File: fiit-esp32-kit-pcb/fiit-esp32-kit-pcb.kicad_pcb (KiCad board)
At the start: 2 copper layers, 25.4 x 75 mm, 79 parts, among them J1 Conn_01x22_Pin, J2 Conn_01x22_Pin, J3 Conn_ARM_JTAG_SWD_10, J4 Conn_01x06_Pin, J5 USB_C_Receptacle_USB2.0, J6 USB_C_Receptacle_USB2.0, Q1 MMDT3904, Q2 SFH320, SW1 SPST NO, SW2 SPST NO, SW3 SPST NO, SW4 SPST NO, SW5 SPST NO, U1 ESP32-S3-WROOM-1, U2 SY8089AAAC, U3 CP2102N-Axx-xQFN28, U4 AHT20

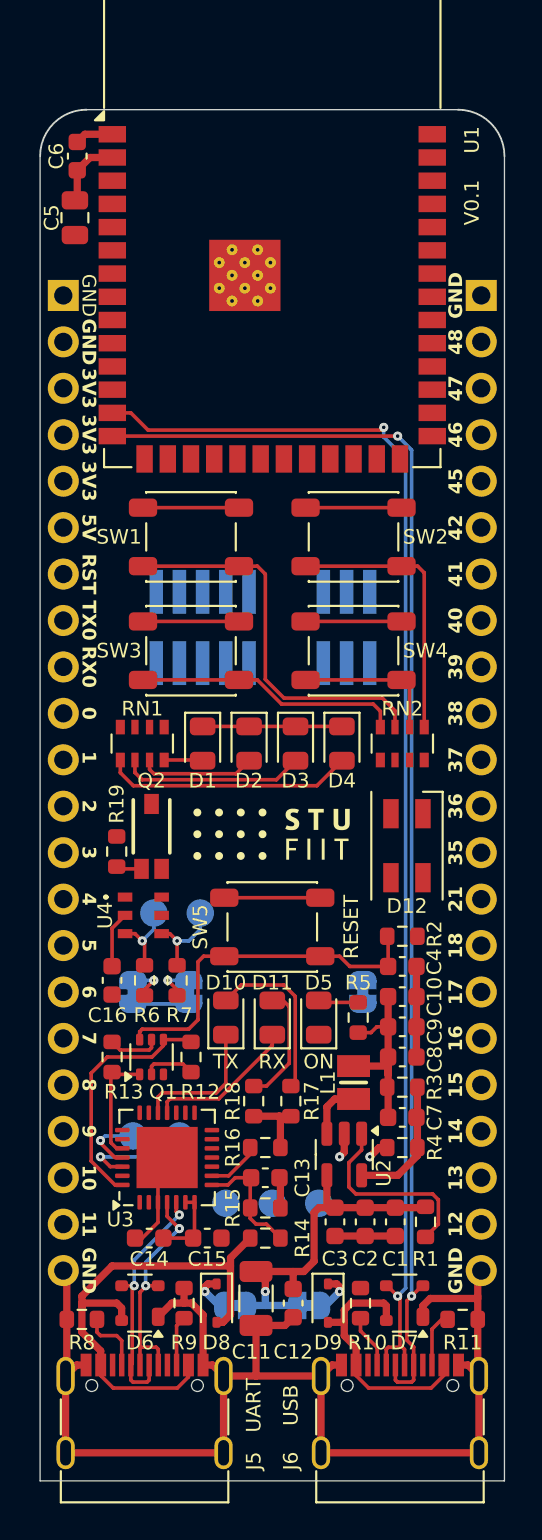
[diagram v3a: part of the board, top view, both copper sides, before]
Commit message: added some tracks (unrouted 76)
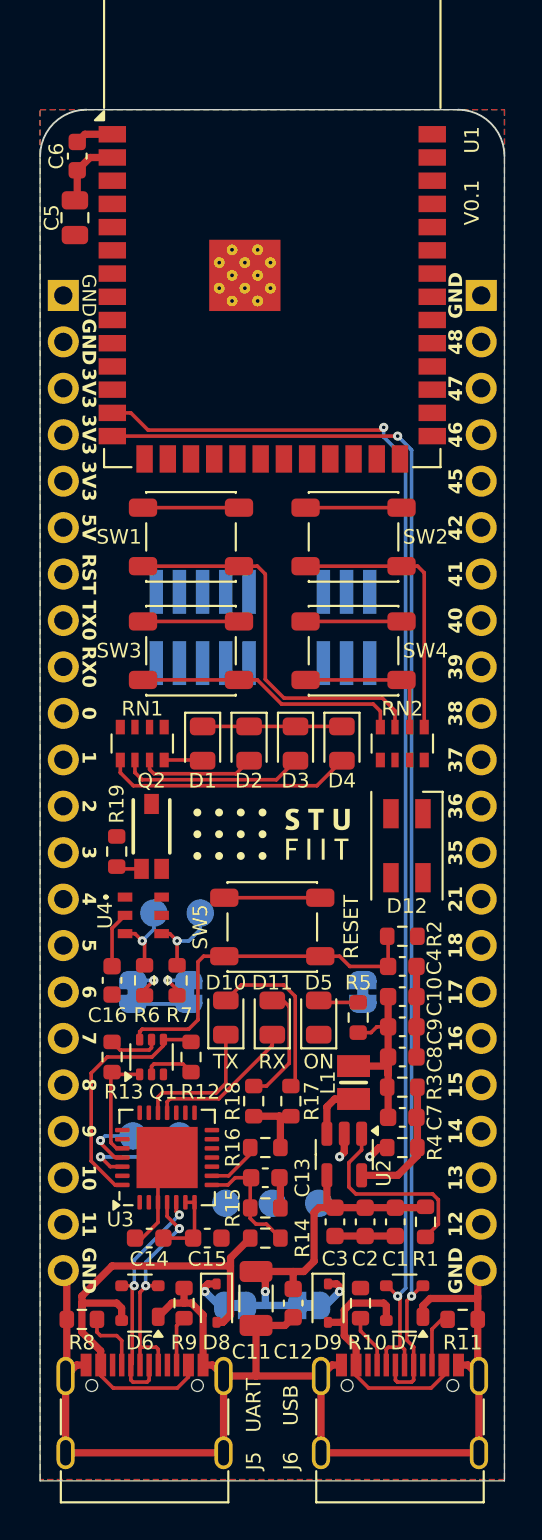
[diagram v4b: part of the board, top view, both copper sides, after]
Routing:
- added copper zone on B.Cu, net GND
- added copper zone on F.Cu, net GND
- added copper zone on In1.Cu, net GND
- added copper zone on In2.Cu, net GND
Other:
- copper layers 2 -> 4
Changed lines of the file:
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@@
 	(layers
 		(0 "F.Cu" signal)
+		(1 "In1.Cu" signal)
+		(2 "In2.Cu" signal)
 		(31 "B.Cu" signal)
 		(32 "B.Adhes" user "B.Adhesive")
@@
 			)
 			(layer "dielectric 1"
+				(type "prepreg")
+				(thickness 0.1)
+				(material "FR4")
+				(epsilon_r 4.5)
+				(loss_tangent 0.02)
+			)
+			(layer "In1.Cu"
+				(type "copper")
+				(thickness 0.035)
+			)
+			(layer "dielectric 2"
 				(type "core")
-				(thickness 1.51)
+				(thickness 1.24)
+				(material "FR4")
+				(epsilon_r 4.5)
+				(loss_tangent 0.02)
+			)
+			(layer "In2.Cu"
+				(type "copper")
+				(thickness 0.035)
+			)
+			(layer "dielectric 3"
+				(type "prepreg")
+				(thickness 0.1)
 				(material "FR4")
 				(epsilon_r 4.5)
@@
 			(size 1.7 1.7)
 			(drill 1)
-			(layers "F&B.Cu" "*.Mask")
+			(layers "*.Cu" "*.Mask")
 			(remove_unused_layers no)
 			(net 2 "GND")
@@
 			(size 1.7 1.7)
 			(drill 1)
-			(layers "F&B.Cu" "*.Mask")
+			(layers "*.Cu" "*.Mask")
 			(remove_unused_layers no)
 			(net 41 "/BUTTON4")
@@
 			(size 1.7 1.7)
 			(drill 1)
-			(layers "F&B.Cu" "*.Mask")
+			(layers "*.Cu" "*.Mask")
 			(remove_unused_layers no)
 			(net 38 "/BUTTON3")
@@
 			(size 1.7 1.7)
 			(drill 1)
-			(layers "F&B.Cu" "*.Mask")
+			(layers "*.Cu" "*.Mask")
 			(remove_unused_layers no)
 			(net 37 "/GPIO46")
@@
 			(size 1.7 1.7)
 			(drill 1)
-			(layers "F&B.Cu" "*.Mask")
+			(layers "*.Cu" "*.Mask")
 			(remove_unused_layers no)
 			(net 42 "/GPIO45")
@@
 			(size 1.7 1.7)
 			(drill 1)
-			(layers "F&B.Cu" "*.Mask")
+			(layers "*.Cu" "*.Mask")
 			(remove_unused_layers no)
 			(net 40 "/GPIO42")
@@
 			(size 1.7 1.7)
 			(drill 1)
-			(layers "F&B.Cu" "*.Mask")
+			(layers "*.Cu" "*.Mask")
 			(remove_unused_layers no)
 			(net 54 "/GPIO41")
@@
 			(size 1.7 1.7)
 			(drill 1)
-			(layers "F&B.Cu" "*.Mask")
+			(layers "*.Cu" "*.Mask")
 			(remove_unused_layers no)
 			(net 39 "/GPIO40")
@@
 			(size 1.7 1.7)
 			(drill 1)
-			(layers "F&B.Cu" "*.Mask")
+			(layers "*.Cu" "*.Mask")
 			(remove_unused_layers no)
 			(net 48 "/GPIO39")
@@
 			(size 1.7 1.7)
 			(drill 1)
-			(layers "F&B.Cu" "*.Mask")
+			(layers "*.Cu" "*.Mask")
 			(remove_unused_layers no)
 			(net 22 "/GPIO38")
@@
 			(size 1.7 1.7)
 			(drill 1)
-			(layers "F&B.Cu" "*.Mask")
+			(layers "*.Cu" "*.Mask")
 			(remove_unused_layers no)
 			(net 43 "/GPIO37")
@@
 			(size 1.7 1.7)
 			(drill 1)
-			(layers "F&B.Cu" "*.Mask")
+			(layers "*.Cu" "*.Mask")
 			(remove_unused_layers no)
 			(net 45 "/GPIO36")
@@
 			(size 1.7 1.7)
 			(drill 1)
-			(layers "F&B.Cu" "*.Mask")
+			(layers "*.Cu" "*.Mask")
 			(remove_unused_layers no)
 			(net 55 "/GPIO35")
@@
 			(size 1.7 1.7)
 			(drill 1)
-			(layers "F&B.Cu" "*.Mask")
+			(layers "*.Cu" "*.Mask")
 			(remove_unused_layers no)
 			(net 53 "/GPIO21")
@@
 			(size 1.7 1.7)
 			(drill 1)
-			(layers "F&B.Cu" "*.Mask")
+			(layers "*.Cu" "*.Mask")
 			(remove_unused_layers no)
 			(net 47 "/GPIO18")
@@
 			(size 1.7 1.7)
 			(drill 1)
-			(layers "F&B.Cu" "*.Mask")
+			(layers "*.Cu" "*.Mask")
 			(remove_unused_layers no)
 			(net 44 "/GPIO17")
@@
 			(size 1.7 1.7)
 			(drill 1)
-			(layers "F&B.Cu" "*.Mask")
+			(layers "*.Cu" "*.Mask")
 			(remove_unused_layers no)
 			(net 52 "/GPIO16")
@@
 			(size 1.7 1.7)
 			(drill 1)
-			(layers "F&B.Cu" "*.Mask")
+			(layers "*.Cu" "*.Mask")
 			(remove_unused_layers no)
 			(net 46 "/GPIO15")
@@
 			(size 1.7 1.7)
 			(drill 1)
-			(layers "F&B.Cu" "*.Mask")
+			(layers "*.Cu" "*.Mask")
 			(remove_unused_layers no)
 			(net 50 "/GPIO14")
@@
 			(size 1.7 1.7)
 			(drill 1)
-			(layers "F&B.Cu" "*.Mask")
+			(layers "*.Cu" "*.Mask")
 			(remove_unused_layers no)
 			(net 51 "/GPIO13")
@@
 			(size 1.7 1.7)
 			(drill 1)
-			(layers "F&B.Cu" "*.Mask")
+			(layers "*.Cu" "*.Mask")
 			(remove_unused_layers no)
 			(net 49 "/GPIO12")
@@
 			(size 1.7 1.7)
 			(drill 1)
-			(layers "F&B.Cu" "*.Mask")
+			(layers "*.Cu" "*.Mask")
 			(remove_unused_layers no)
 			(net 2 "GND")
@@
 			(size 1.7 1.7)
 			(drill 1)
-			(layers "F&B.Cu" "*.Mask")
+			(layers "*.Cu" "*.Mask")
 			(remove_unused_layers no)
 			(net 2 "GND")
@@
 			(size 1.7 1.7)
 			(drill 1)
-			(layers "F&B.Cu" "*.Mask")
+			(layers "*.Cu" "*.Mask")
 			(remove_unused_layers no)
 			(net 2 "GND")
@@
 			(size 1.7 1.7)
 			(drill 1)
-			(layers "F&B.Cu" "*.Mask")
+			(layers "*.Cu" "*.Mask")
 			(remove_unused_layers no)
 			(net 1 "+3.3V")
@@
 			(size 1.7 1.7)
 			(drill 1)
-			(layers "F&B.Cu" "*.Mask")
+			(layers "*.Cu" "*.Mask")
 			(remove_unused_layers no)
 			(net 1 "+3.3V")
@@
 			(size 1.7 1.7)
 			(drill 1)
-			(layers "F&B.Cu" "*.Mask")
+			(layers "*.Cu" "*.Mask")
 			(remove_unused_layers no)
 			(net 1 "+3.3V")
@@
 			(size 1.7 1.7)
 			(drill 1)
-			(layers "F&B.Cu" "*.Mask")
+			(layers "*.Cu" "*.Mask")
 			(remove_unused_layers no)
 			(net 4 "+5V")
@@
 			(size 1.7 1.7)
 			(drill 1)
-			(layers "F&B.Cu" "*.Mask")
+			(layers "*.Cu" "*.Mask")
 			(remove_unused_layers no)
 			(net 3 "/EN")
@@
 			(size 1.7 1.7)
 			(drill 1)
-			(layers "F&B.Cu" "*.Mask")
+			(layers "*.Cu" "*.Mask")
 			(remove_unused_layers no)
 			(net 28 "/TX0")
@@
 			(size 1.7 1.7)
 			(drill 1)
-			(layers "F&B.Cu" "*.Mask")
+			(layers "*.Cu" "*.Mask")
 			(remove_unused_layers no)
 			(net 30 "/RX0")
@@
 			(size 1.7 1.7)
 			(drill 1)
-			(layers "F&B.Cu" "*.Mask")
+			(layers "*.Cu" "*.Mask")
 			(remove_unused_layers no)
 			(net 27 "/BOOT")
@@
 			(size 1.7 1.7)
 			(drill 1)
-			(layers "F&B.Cu" "*.Mask")
+			(layers "*.Cu" "*.Mask")
 			(remove_unused_layers no)
 			(net 24 "/BUTTON1")
@@
 			(size 1.7 1.7)
 			(drill 1)
-			(layers "F&B.Cu" "*.Mask")
+			(layers "*.Cu" "*.Mask")
 			(remove_unused_layers no)
 			(net 34 "/BUTTON2")
@@
 			(size 1.7 1.7)
 			(drill 1)
-			(layers "F&B.Cu" "*.Mask")
+			(layers "*.Cu" "*.Mask")
 			(remove_unused_layers no)
 			(net 26 "/GPIO3")
@@
 			(size 1.7 1.7)
 			(drill 1)
-			(layers "F&B.Cu" "*.Mask")
+			(layers "*.Cu" "*.Mask")
 			(remove_unused_layers no)
 			(net 31 "/GPIO4")
@@
 			(size 1.7 1.7)
 			(drill 1)
-			(layers "F&B.Cu" "*.Mask")
+			(layers "*.Cu" "*.Mask")
 			(remove_unused_layers no)
 			(net 29 "/GPIO5")
@@
 			(size 1.7 1.7)
 			(drill 1)
-			(layers "F&B.Cu" "*.Mask")
+			(layers "*.Cu" "*.Mask")
 			(remove_unused_layers no)
 			(net 23 "/GPIO6")
@@
 			(size 1.7 1.7)
 			(drill 1)
-			(layers "F&B.Cu" "*.Mask")
+			(layers "*.Cu" "*.Mask")
 			(remove_unused_layers no)
 			(net 33 "/GPIO7")
@@
 			(size 1.7 1.7)
 			(drill 1)
-			(layers "F&B.Cu" "*.Mask")
+			(layers "*.Cu" "*.Mask")
 			(remove_unused_layers no)
 			(net 25 "/GPIO8")
@@
 			(size 1.7 1.7)
 			(drill 1)
-			(layers "F&B.Cu" "*.Mask")
+			(layers "*.Cu" "*.Mask")
 			(remove_unused_layers no)
 			(net 35 "/GPIO9")
@@
 			(size 1.7 1.7)
 			(drill 1)
-			(layers "F&B.Cu" "*.Mask")
+			(layers "*.Cu" "*.Mask")
 			(remove_unused_layers no)
 			(net 32 "/GPIO10")
@@
 			(size 1.7 1.7)
 			(drill 1)
-			(layers "F&B.Cu" "*.Mask")
+			(layers "*.Cu" "*.Mask")
 			(remove_unused_layers no)
 			(net 36 "/GPIO11")
@@
 			(size 1.7 1.7)
 			(drill 1)
-			(layers "F&B.Cu" "*.Mask")
+			(layers "*.Cu" "*.Mask")
 			(remove_unused_layers no)
 			(net 2 "GND")
@@
 		(net 96)
 	)
+	(zone
+		(net 2)
+		(net_name "GND")
+		(layers "F.Cu" "In1.Cu" "In2.Cu" "B.Cu")
+		(hatch edge 0.5)
+		(priority 1)
+		(connect_pads
+			(clearance 0.2)
+		)
+		(min_thickness 0.2)
+		(filled_areas_thickness no)
+		(fill yes
+			(thermal_gap 0.2)
+			(thermal_bridge_width 0.25)
+		)
+		(polygon
+			(pts
+				(xy 195 48.15) (xy 220.4 48.15) (xy 220.4 123.08) (xy 195 123.08)
+			)
+		)
+	)
 	(group ""

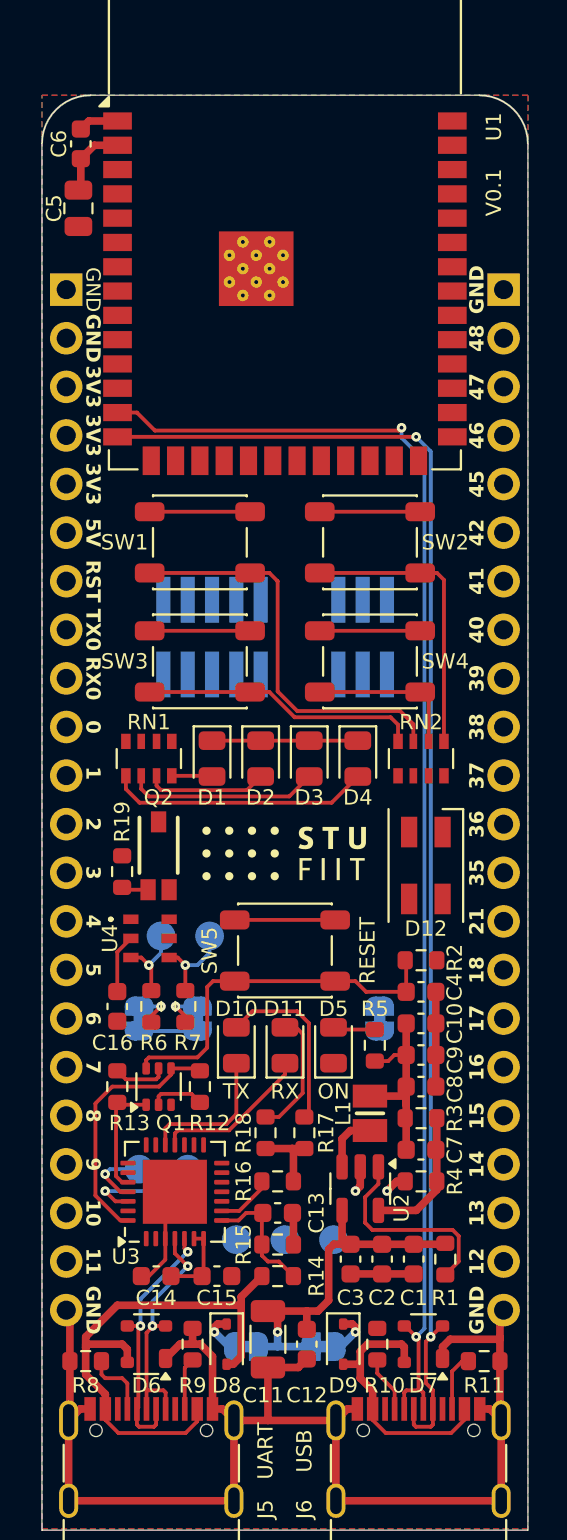
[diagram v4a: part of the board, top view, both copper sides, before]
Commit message: added some tracks (unrouted 0 !!!)
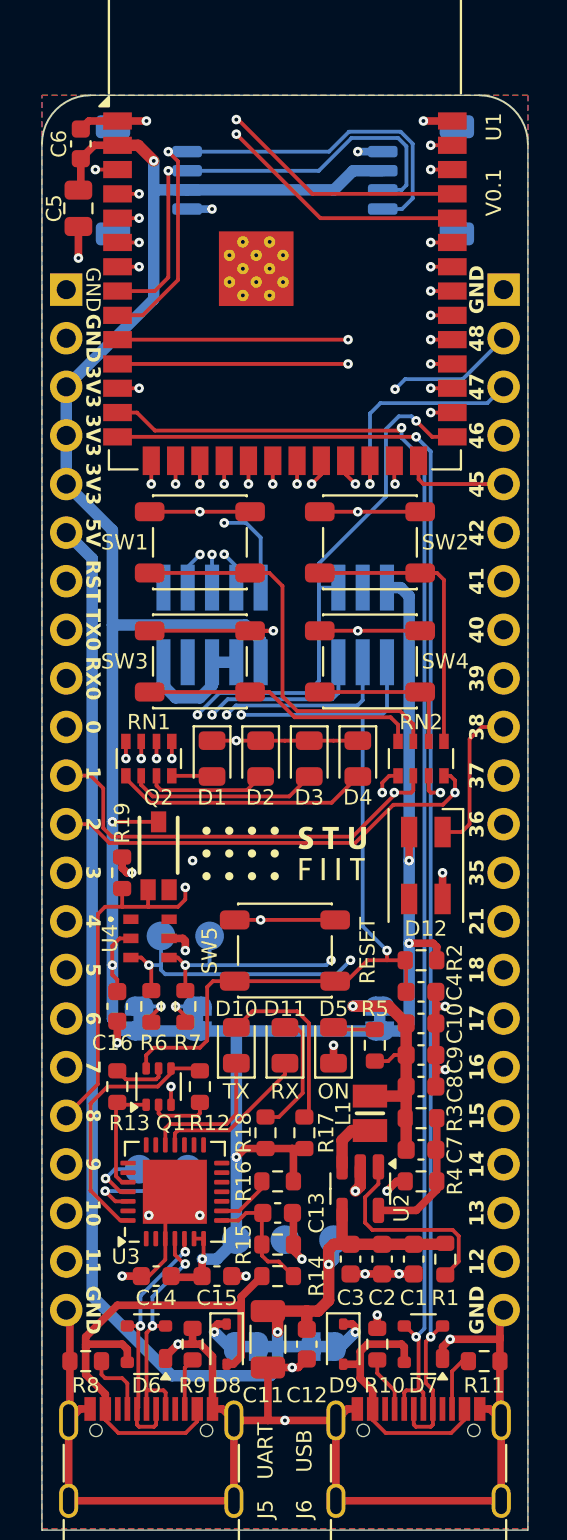
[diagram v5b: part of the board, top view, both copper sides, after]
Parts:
- added J7: QWIIC - I2C, Connector_JST:JST_SH_SM04B-SRSS-TB_1x04-1MP_P1.00mm_Horizontal, B.Cu at (200.6, 52.6)
- added J8: QWIIC - I2C, Connector_JST:JST_SH_SM04B-SRSS-TB_1x04-1MP_P1.00mm_Horizontal, B.Cu at (214.8, 52.6)
- moved J3 0.64 mm to (203.9, 75.8)
- moved J4 0.64 mm to (211.8, 75.8)
- moved R19 0.06 mm to (199.2, 88.8)
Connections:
- RN1 pad 5: /GPIO4 -> /GPIO7
- RN1 pad 6: /GPIO5 -> /GPIO6
- RN1 pad 7: /GPIO6 -> /GPIO5
- RN1 pad 8: /GPIO7 -> /GPIO4
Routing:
- net +3.3V: track 17.9 -> 147.6 mm, vias 0 -> 7
- net /GPIO16: track 4.28 -> 102.8 mm, vias 1 -> 3
- net /GPIO15: track 4.77 -> 100.9 mm, vias 1 -> 3
- net /RX0: track 6.21 -> 99.3 mm, vias 1 -> 3
- net /TX0: track 3.54 -> 95.8 mm, vias 1 -> 3
- net /BUTTON2: track 0.00 -> 60.5 mm, vias 0 -> 2
- net /EN: track 19.5 -> 79.0 mm, vias 0 -> 3
- net /BUTTON1: track 0.00 -> 58.9 mm, vias 0 -> 2
- net /BOOT: track 0.00 -> 55.7 mm, vias 0 -> 3
- net +5V: track 19.9 -> 74.2 mm, vias 1 -> 2
- net /GPIO17: track 0.00 -> 54.0 mm, vias 0 -> 1
- net /GPIO11: track 0.00 -> 49.4 mm, vias 0 -> 1
- net /GPIO9: track 0.00 -> 48.4 mm, vias 0 -> 1
- net /GPIO18: track 0.00 -> 48.1 mm, vias 0 -> 1
- net /GPIO12: track 0.00 -> 47.7 mm, vias 0 -> 1
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
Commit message: final improvements
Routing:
- net GND: vias 32 -> 114
